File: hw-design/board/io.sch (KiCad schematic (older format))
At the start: 12 parts, among them P3 CONN_01X02, P4 CONN_01X03, SW1 SP3T

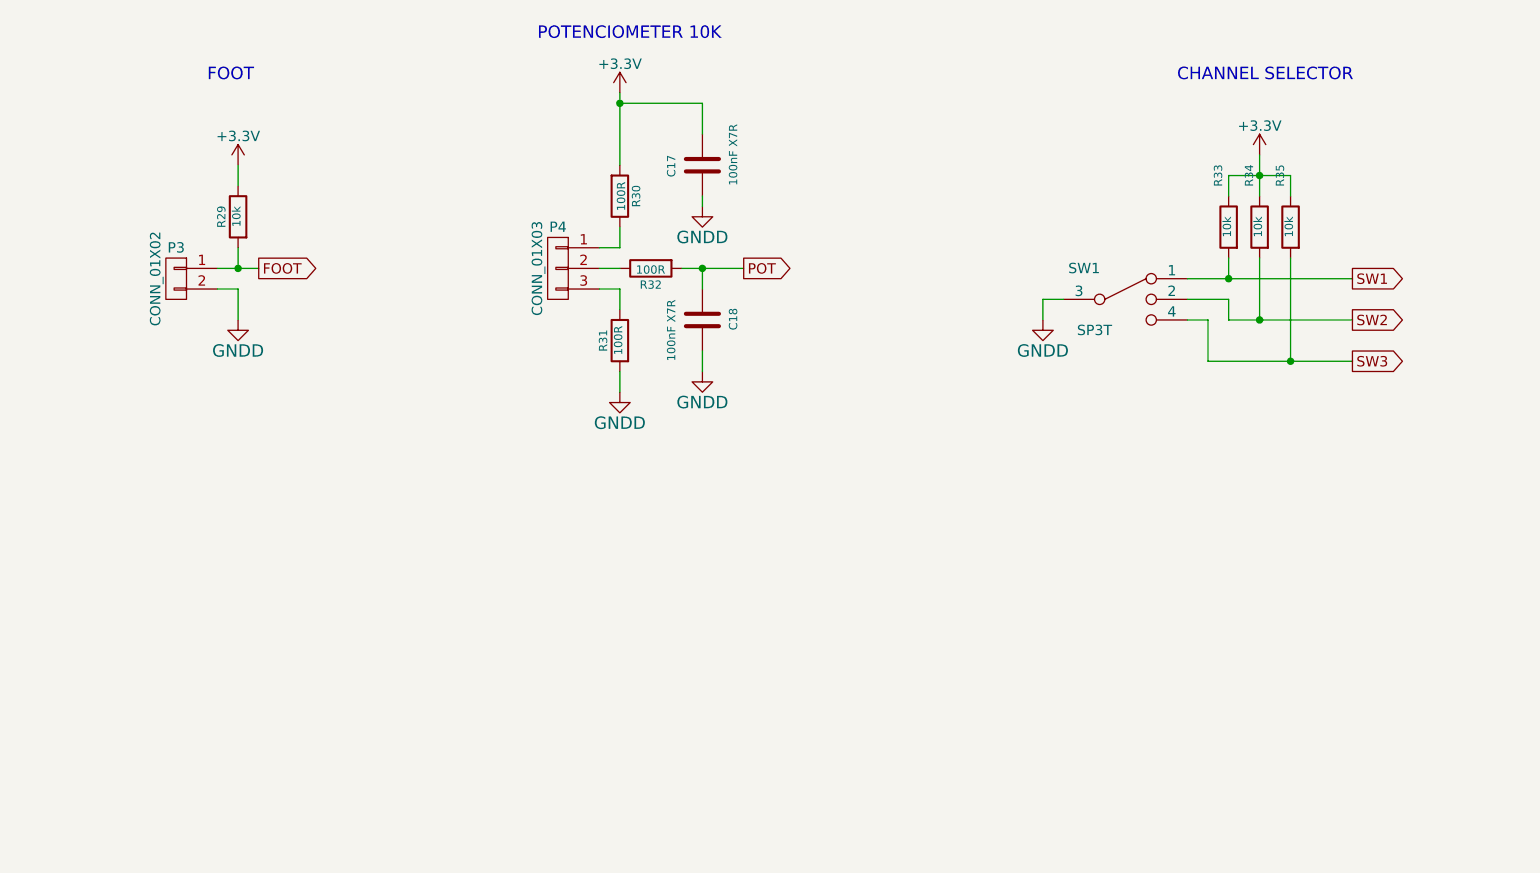
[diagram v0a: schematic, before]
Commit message: sch: cpu, I/Os and control chain circuits done
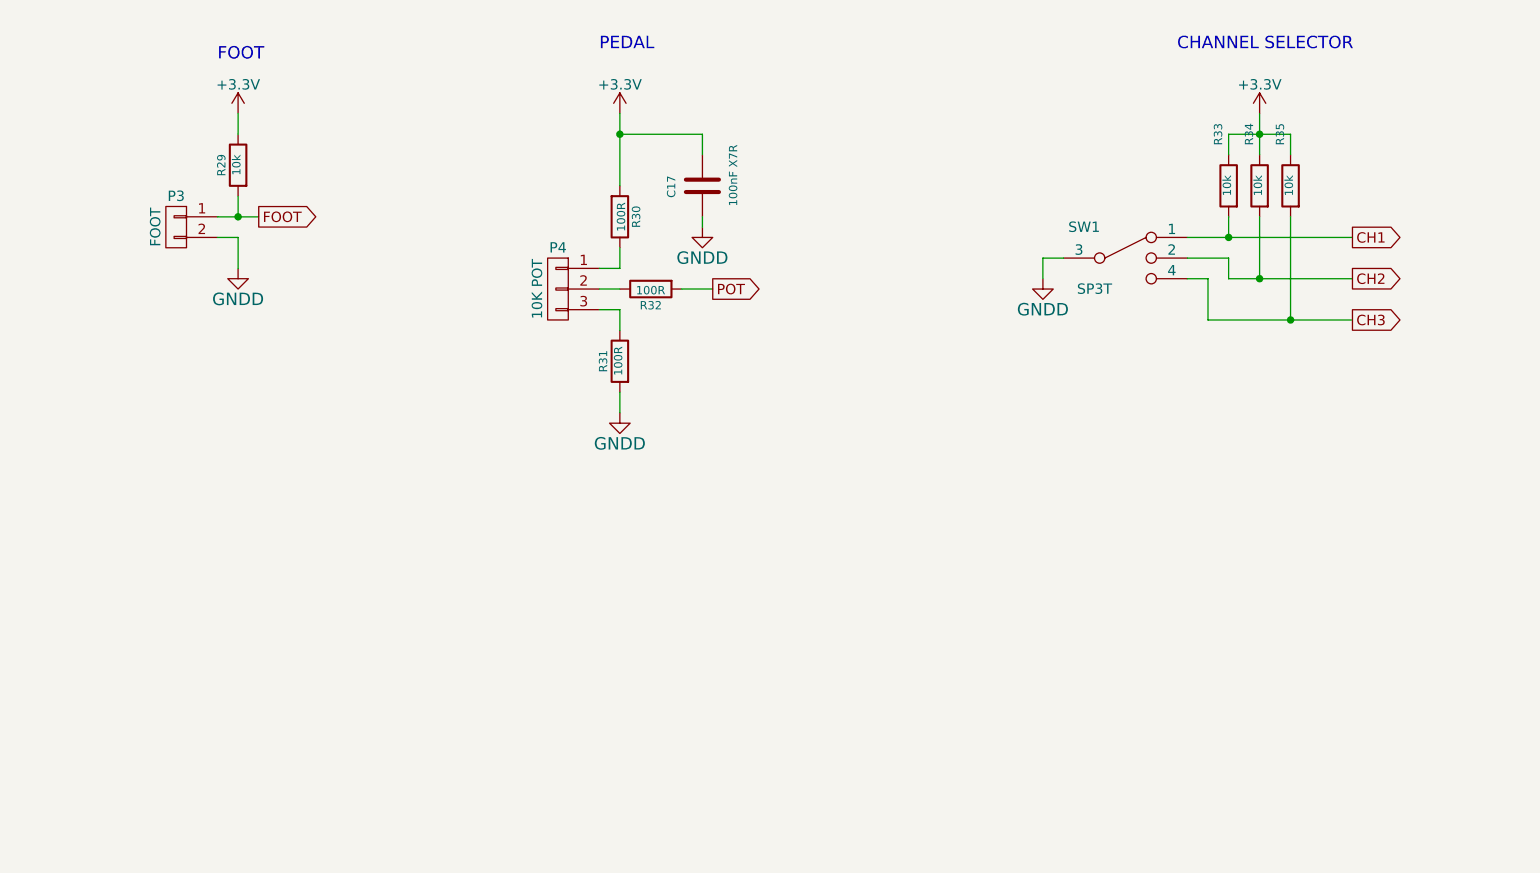
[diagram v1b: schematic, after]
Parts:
- removed C18: 100nF X7R, Capacitors_SMD:C_0603, symbol C
- P3: value CONN_01X02 -> FOOT
- P4: value CONN_01X03 -> 10K POT
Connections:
- net SW1 renamed CH1
- net SW2 renamed CH2
- net SW3 renamed CH3
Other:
- note added: "PEDAL"
- note removed: "POTENCIOMETER 10K"
- moved on the sheet: C17, P3, P4, R29, R30, R31, R32, R33, R34, R35, SW1

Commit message: sch: schematic annotation done
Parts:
- added C17: 100nF X7R, Capacitors_SMD:C_0603, symbol C
- added D5: LED_RGB, symbol LED_RGB
- added R22, R23, R24: 220R, Resistors_SMD:R_0603, symbol R
- renumbered C17 to C18, P3 to P4, P4 to P5, R29 to R25, R30 to R26, R31 to R27, R32 to R28, R33 to R29, R34 to R30, R35 to R31, SW1 to SW2
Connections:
- net +3V3: now also C17.2, D5.BA (BLUE_ANODE), D5.GA (GREEN_ANODE), D5.RA (RED_ANODE)
- net GNDD: now also C17.1
- net FOOT renamed FS1
- new net: D5.RC (RED_CATHODE), R22.2
- new net: D5.BC (BLUE_CATHODE), R24.2
- new net: D5.GC (GREEN_CATHODE), R23.2
- new net FS1_LED_B: R24.1
- new net FS1_LED_G: R23.1
- new net FS1_LED_R: R22.1
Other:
- note added: "LED"
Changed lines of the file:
@@
 $EndDescr
 $Comp
-L R R33
+L R R29
 U 1 1 54CBEC23
 P 6850 1750
-F 0 "R33" V 6900 2000 40  0000 C CNN
+F 0 "R29" V 6900 2000 40  0000 C CNN
 F 1 "10k" V 6857 1751 40  0000 C CNN
 F 2 "Resistors_SMD:R_0603" V 6780 1750 30  0001 C CNN
@@
 $EndComp
 $Comp
-L R R34
+L R R30
 U 1 1 54CBEC30
 P 7000 1750
-F 0 "R34" V 7050 2000 40  0000 C CNN
+F 0 "R30" V 7050 2000 40  0000 C CNN
 F 1 "10k" V 7007 1751 40  0000 C CNN
 F 2 "Resistors_SMD:R_0603" V 6930 1750 30  0001 C CNN
@@
 $EndComp
 $Comp
-L R R35
+L R R31
 U 1 1 54CBEC37
 P 7150 1750
-F 0 "R35" V 7200 2000 40  0000 C CNN
+F 0 "R31" V 7200 2000 40  0000 C CNN
 F 1 "10k" V 7157 1751 40  0000 C CNN
 F 2 "Resistors_SMD:R_0603" V 7080 1750 30  0001 C CNN
@@
 $EndComp
 $Comp
-L R R29
+L R R25
 U 1 1 54CBEC53
 P 2050 1650
-F 0 "R29" V 2130 1650 40  0000 C CNN
+F 0 "R25" V 2130 1650 40  0000 C CNN
 F 1 "10k" V 2057 1651 40  0000 C CNN
 F 2 "Resistors_SMD:R_0603" V 1980 1650 30  0001 C CNN
@@
 $EndComp
 Text GLabel 2150 1900 2    50   Output ~ 0
-FOOT
+FS1
 Text GLabel 7450 2000 2    50   Output ~ 0
 CH1
@@
 CH3
 $Comp
-L R R30
+L R R26
 U 1 1 54CBEC6F
 P 3900 1900
-F 0 "R30" V 3980 1900 40  0000 C CNN
+F 0 "R26" V 3980 1900 40  0000 C CNN
 F 1 "100R" V 3907 1901 40  0000 C CNN
 F 2 "Resistors_SMD:R_0603" V 3830 1900 30  0001 C CNN
@@
 $EndComp
 $Comp
-L R R31
+L R R27
 U 1 1 54CBEC82
 P 3900 2600
-F 0 "R31" V 3980 2600 40  0000 C CNN
+F 0 "R27" V 3980 2600 40  0000 C CNN
 F 1 "100R" V 3907 2601 40  0000 C CNN
 F 2 "Resistors_SMD:R_0603" V 3830 2600 30  0001 C CNN
@@
 $EndComp
 $Comp
-L R R32
+L R R28
 U 1 1 54CBEC89
 P 4050 2250
-F 0 "R32" V 4130 2250 40  0000 C CNN
+F 0 "R28" V 4130 2250 40  0000 C CNN
 F 1 "100R" V 4057 2251 40  0000 C CNN
 F 2 "Resistors_SMD:R_0603" V 3980 2250 30  0001 C CNN
@@
 Text GLabel 4350 2250 2    50   Output ~ 0
 POT
-Text Notes 3800 1100 0    60   ~ 0
+Text Notes 3800 1100 0    100  ~ 0
 PEDAL
-Text Notes 6600 1100 0    60   ~ 0
+Text Notes 6600 1100 0    100  ~ 0
 CHANNEL SELECTOR
-Text Notes 1950 1150 0    60   ~ 0
+Text Notes 1950 1150 0    100  ~ 0
 FOOT
 $Comp
-L C C17
+L C C18
 U 1 1 54CBECAC
 P 4300 1750
-F 0 "C17" V 4150 1700 40  0000 L CNN
+F 0 "C18" V 4150 1700 40  0000 L CNN
 F 1 "100nF X7R" V 4450 1550 40  0000 L CNN
 F 2 "Capacitors_SMD:C_0603" H 4338 1600 30  0001 C CNN
@@
 $EndComp
 $Comp
-L GNDD #PWR060
+L GNDD #PWR055
 U 1 1 54E65047
 P 2050 2150
-F 0 "#PWR060" H 2050 1900 60  0001 C CNN
+F 0 "#PWR055" H 2050 1900 60  0001 C CNN
 F 1 "GNDD" H 2050 2000 60  0000 C CNN
 F 2 "" H 2050 2150 60  0000 C CNN
@@
 $EndComp
 $Comp
-L GNDD #PWR062
+L GNDD #PWR056
 U 1 1 54E661EA
 P 3900 2850
-F 0 "#PWR062" H 3900 2600 60  0001 C CNN
+F 0 "#PWR056" H 3900 2600 60  0001 C CNN
 F 1 "GNDD" H 3900 2700 60  0000 C CNN
 F 2 "" H 3900 2850 60  0000 C CNN
@@
 $EndComp
 $Comp
-L GNDD #PWR065
+L GNDD #PWR057
 U 1 1 54E66D8A
 P 4300 1950
-F 0 "#PWR065" H 4300 1700 60  0001 C CNN
+F 0 "#PWR057" H 4300 1700 60  0001 C CNN
 F 1 "GNDD" H 4300 1800 60  0000 C CNN
 F 2 "" H 4300 1950 60  0000 C CNN
@@
 $EndComp
 $Comp
-L CONN_01X02 P3
+L CONN_01X02 P4
 U 1 1 54E6B5CA
 P 1750 1950
-F 0 "P3" H 1750 2100 50  0000 C CNN
+F 0 "P4" H 1750 2100 50  0000 C CNN
 F 1 "FOOT" V 1850 1950 50  0000 C CNN
 F 2 "Pin_Headers:Pin_Header_Straight_1x02" H 1750 1950 60  0001 C CNN
@@
 $EndComp
 $Comp
-L CONN_01X03 P4
+L CONN_01X03 P5
 U 1 1 54E6CA4C
 P 3600 2250
-F 0 "P4" H 3600 2450 50  0000 C CNN
+F 0 "P5" H 3600 2450 50  0000 C CNN
 F 1 "10K POT" V 3700 2250 50  0000 C CNN
 F 2 "Pin_Headers:Pin_Header_Straight_1x03" H 3600 2250 60  0001 C CNN
@@
 $EndComp
 $Comp
-L SP3T SW1
+L SP3T SW2
 U 1 1 54E74297
 P 6350 2100
-F 0 "SW1" H 6150 2250 50  0000 C CNN
+F 0 "SW2" H 6150 2250 50  0000 C CNN
 F 1 "SP3T" H 6200 1950 50  0000 C CNN
 F 2 "MOD_Footprints:SWITCH_HH_SK-13D26-G-6_5-K-GY" H 6350 2100 60  0001 C CNN
@@
 $EndComp
 $Comp
-L GNDD #PWR067
+L GNDD #PWR058
 U 1 1 54E753B2
 P 5950 2200
-F 0 "#PWR067" H 5950 1950 60  0001 C CNN
+F 0 "#PWR058" H 5950 1950 60  0001 C CNN
 F 1 "GNDD" H 5950 2050 60  0000 C CNN
 F 2 "" H 5950 2200 60  0000 C CNN
@@
 	7150 1500 7150 1600
 Wire Wire Line
-	6850 1500 7000 1500
-Wire Wire Line
-	7000 1500 7150 1500
+	6850 1500 7150 1500
 Wire Wire Line
 	6850 1500 6850 1600
 Wire Wire Line
-	7000 1400 7000 1500
-Wire Wire Line
-	7000 1500 7000 1600
+	7000 1400 7000 1600
 Connection ~ 7000 1500
 Wire Wire Line
-	6650 2000 6850 2000
-Wire Wire Line
-	6850 2000 7450 2000
-Wire Wire Line
-	6850 2200 7000 2200
-Wire Wire Line
-	7000 2200 7450 2200
-Wire Wire Line
-	6750 2400 7150 2400
-Wire Wire Line
-	7150 2400 7450 2400
+	6650 2000 7450 2000
+Wire Wire Line
+	6850 2200 7450 2200
+Wire Wire Line
+	6750 2400 7450 2400
 Wire Wire Line
 	6850 1900 6850 2000
@@
 	2050 1800 2050 1900
 Wire Wire Line
-	1950 1900 2050 1900
-Wire Wire Line
-	2050 1900 2150 1900
+	1950 1900 2150 1900
 Wire Wire Line
 	2050 1400 2050 1500
@@
 	2050 2000 2050 2150
 Wire Wire Line
-	3900 1400 3900 1500
-Wire Wire Line
-	3900 1500 3900 1750
+	3900 1400 3900 1750
 Wire Wire Line
 	4300 1600 4300 1500
@@
 	4300 1900 4300 1950
 $Comp
-L +3.3V #PWR?
+L +3.3V #PWR059
 U 1 1 556F3C3C
 P 2050 1400
-F 0 "#PWR?" H 2050 1250 50  0001 C CNN
+F 0 "#PWR059" H 2050 1250 50  0001 C CNN
 F 1 "+3.3V" H 2050 1540 50  0000 C CNN
 F 2 "" H 2050 1400 60  0000 C CNN
@@
 $EndComp
 $Comp
-L +3.3V #PWR?
+L +3.3V #PWR060
 U 1 1 556F3CC5
 P 3900 1400
-F 0 "#PWR?" H 3900 1250 50  0001 C CNN
+F 0 "#PWR060" H 3900 1250 50  0001 C CNN
 F 1 "+3.3V" H 3900 1540 50  0000 C CNN
 F 2 "" H 3900 1400 60  0000 C CNN
@@
 $EndComp
 $Comp
-L +3.3V #PWR?
+L +3.3V #PWR061
 U 1 1 556F428C
 P 7000 1400
-F 0 "#PWR?" H 7000 1250 50  0001 C CNN
+F 0 "#PWR061" H 7000 1250 50  0001 C CNN
 F 1 "+3.3V" H 7000 1540 50  0000 C CNN
 F 2 "" H 7000 1400 60  0000 C CNN
@@
 Wire Wire Line
 	4200 2250 4350 2250
+Text Notes 2350 3900 0    100  ~ 0
+LED
+$Comp
+L C C17
+U 1 1 557A9E0C
+P 3150 4600
+F 0 "C17" V 3100 4450 40  0000 L CNN
+F 1 "100nF X7R" V 3300 4400 40  0000 L CNN
+F 2 "Capacitors_SMD:C_0603" H 3188 4450 30  0001 C CNN
+F 3 "~" H 3150 4600 60  0000 C CNN
+	1    3150 4600
+	1    0    0    1
+$EndComp
+$Comp
+L +3.3V #PWR062
+U 1 1 557A9EA8
+P 2900 4300
+F 0 "#PWR062" H 2900 4150 50  0001 C CNN
+F 1 "+3.3V" H 2900 4440 50  0000 C CNN
+F 2 "" H 2900 4300 60  0000 C CNN
+F 3 "" H 2900 4300 60  0000 C CNN
+	1    2900 4300
+	1    0    0    -1
+$EndComp
+Wire Wire Line
+	2900 4300 2900 4800
+Wire Wire Line
+	2900 4800 2800 4800
+Wire Wire Line
+	2800 4600 2900 4600
+Connection ~ 2900 4600
+Wire Wire Line
+	2800 4400 3150 4400
+Connection ~ 2900 4400
+Wire Wire Line
+	3150 4400 3150 4450
+$Comp
+L GNDD #PWR063
+U 1 1 557AA05D
+P 3150 4800
+F 0 "#PWR063" H 3150 4550 50  0001 C CNN
+F 1 "GNDD" H 3150 4650 50  0000 C CNN
+F 2 "" H 3150 4800 60  0000 C CNN
+F 3 "" H 3150 4800 60  0000 C CNN
+	1    3150 4800
+	1    0    0    -1
+$EndComp
+Wire Wire Line
+	3150 4750 3150 4800
+$Comp
+L R R22
+U 1 1 557AA39A
+P 1950 4400
+F 0 "R22" V 2030 4400 40  0000 C CNN
+F 1 "220R" V 1957 4401 40  0000 C CNN
+F 2 "Resistors_SMD:R_0603" V 1880 4400 30  0001 C CNN
+F 3 "~" H 1950 4400 30  0000 C CNN
+	1    1950 4400
+	0    -1   1    0
+$EndComp
+Wire Wire Line
+	2100 4400 2200 4400
+Wire Wire Line
+	2200 4600 2100 4600
+Wire Wire Line
+	2100 4800 2200 4800
+Text GLabel 1550 4400 0    50   Input ~ 0
+FS1_LED_R
+Wire Wire Line
+	1550 4400 1800 4400
+$Comp
+L LED_RGB D5
+U 1 1 557AAC2C
+P 2500 4600
+F 0 "D5" H 2500 5050 50  0000 C CNN
+F 1 "LED_RGB" H 2500 4950 50  0000 C CNN
+F 2 "" H 2500 4550 60  0000 C CNN
+F 3 "" H 2500 4550 60  0000 C CNN
+	1    2500 4600
+	1    0    0    -1
+$EndComp
+Text GLabel 1550 4600 0    50   Input ~ 0
+FS1_LED_G
+Wire Wire Line
+	1550 4600 1800 4600
+Text GLabel 1550 4800 0    50   Input ~ 0
+FS1_LED_B
+Wire Wire Line
+	1550 4800 1800 4800
+$Comp
+L R R23
+U 1 1 557AADB8
+P 1950 4600
+F 0 "R23" V 2030 4600 40  0000 C CNN
+F 1 "220R" V 1957 4601 40  0000 C CNN
+F 2 "Resistors_SMD:R_0603" V 1880 4600 30  0001 C CNN
+F 3 "~" H 1950 4600 30  0000 C CNN
+	1    1950 4600
+	0    -1   1    0
+$EndComp
+$Comp
+L R R24
+U 1 1 557AAE1B
+P 1950 4800
+F 0 "R24" V 2030 4800 40  0000 C CNN
+F 1 "220R" V 1957 4801 40  0000 C CNN
+F 2 "Resistors_SMD:R_0603" V 1880 4800 30  0001 C CNN
+F 3 "~" H 1950 4800 30  0000 C CNN
+	1    1950 4800
+	0    -1   1    0
+$EndComp
 $EndSCHEMATC

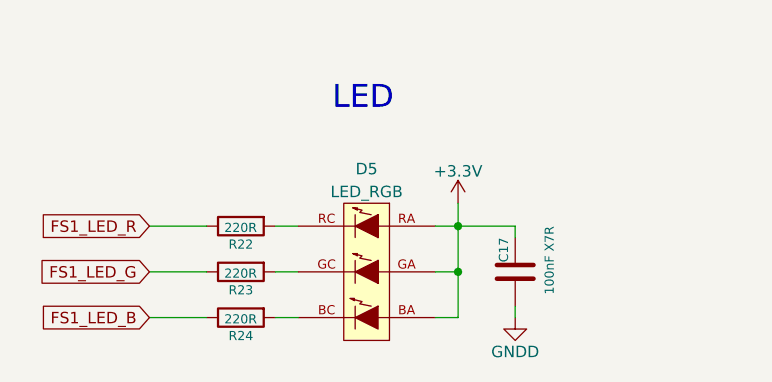
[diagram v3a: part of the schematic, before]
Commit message: sch: adding values and MPN to components
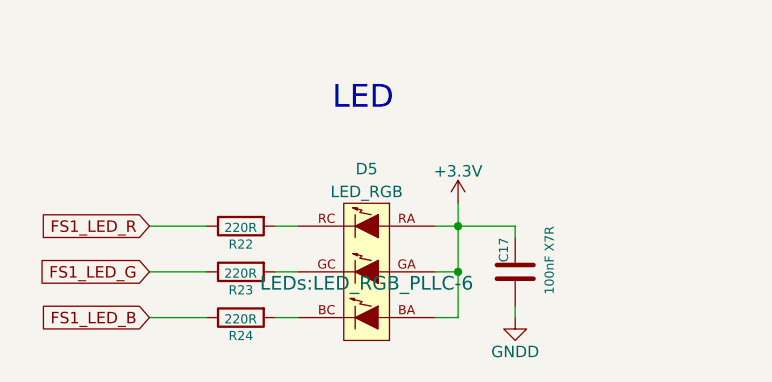
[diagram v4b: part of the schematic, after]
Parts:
- C17, C18: MPN (none) -> C1608X7R1E104K080AA
- D5: footprint (none) -> LEDs:LED_RGB_PLLC-6; MPN (none) -> LTRBGFSF-ABCB-QKYO-Z
- P4: MPN (none) -> M20-9990246
- P5: MPN (none) -> M20-9990346
- R22, R23, R24: MPN (none) -> ESR03EZPJ221
- R25, R29, R30, R31: MPN (none) -> RMCF0603JT10K0
- R26, R27, R28: MPN (none) -> RMCF0603JT100R
- SW2: MPN (none) -> OS103011MA7QP1

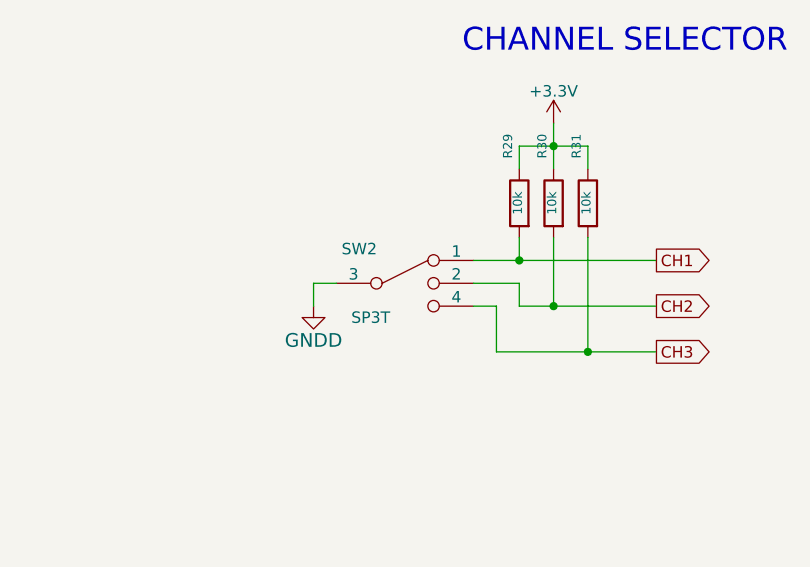
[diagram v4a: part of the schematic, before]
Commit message: fixing some footprints assignment
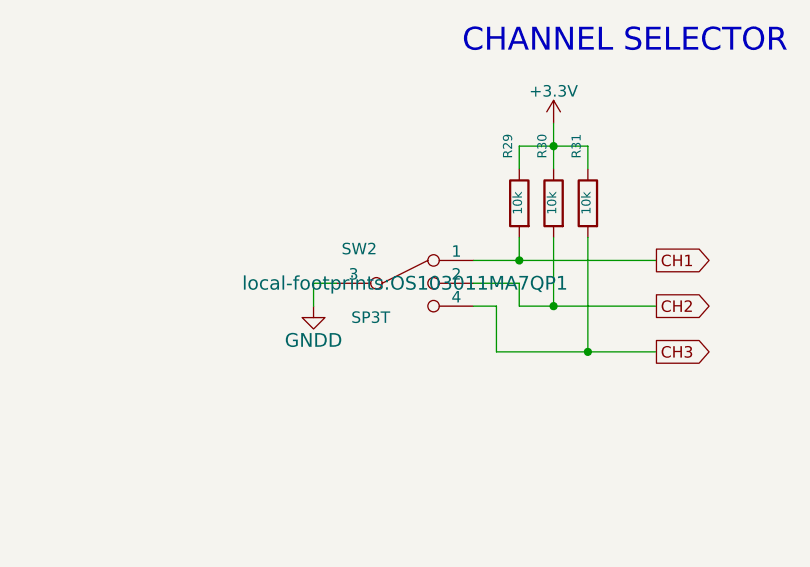
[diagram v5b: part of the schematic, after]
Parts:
- SW2: footprint MOD_Footprints:SWITCH_HH_SK-13D26-G-6_5-K-GY -> local-footprints:OS103011MA7QP1
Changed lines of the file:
@@
 F 0 "SW2" H 6150 2250 50  0000 C CNN
 F 1 "SP3T" H 6200 1950 50  0000 C CNN
-F 2 "MOD_Footprints:SWITCH_HH_SK-13D26-G-6_5-K-GY" H 6350 2100 60  0001 C CNN
+F 2 "local-footprints:OS103011MA7QP1" H 6350 2100 60  0000 C CNN
 F 3 "" H 6350 2100 60  0000 C CNN
 F 4 "OS103011MA7QP1" H 0   0   50  0001 C CNN "MPN"
